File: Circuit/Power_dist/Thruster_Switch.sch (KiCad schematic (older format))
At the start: 7 parts, among them P1 XT60, Q1 IPD90P03P4L

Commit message: refactor Power_dist
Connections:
- net labels added: GNDPWR
- net labels removed: GND
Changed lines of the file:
@@
 	0    1    1    0
-$EndComp
-$Comp
-L GND #PWR026
-U 1 1 58E0369B
-P 6250 4800
-AR Path="/58E52973/58E0369B" Ref="#PWR026"  Part="1"
-AR Path="/58E62AD5/58E0369B" Ref="#PWR023"  Part="1"
-AR Path="/58E0048C/58E0369B" Ref="#PWR029"  Part="1"
-F 0 "#PWR029" H 6250 4550 50  0001 C CNN
-F 1 "GND" H 6250 4650 50  0000 C CNN
-F 2 "" H 6250 4800 50  0001 C CNN
-F 3 "" H 6250 4800 50  0001 C CNN
-	1    6250 4800
-	1    0    0    -1
 $EndComp
 Text HLabel 3700 2300 0    60   Input ~ 0
@@
 	5250 2500 5400 2500
 Connection ~ 5250 3050
-Connection ~ 6650 3850
 Wire Wire Line
 	6250 4450 6250 4300
-Connection ~ 6650 4750
 Wire Wire Line
 	6250 4650 6250 4800
@@
 Wire Wire Line
 	6650 3850 6250 3850
+$Comp
+L GNDPWR #PWR?
+U 1 1 5B5DEA3D
+P 6250 4800
+AR Path="/58E0048C/5B5DEA3D" Ref="#PWR?"  Part="1"
+AR Path="/58E52973/5B5DEA3D" Ref="#PWR?"  Part="1"
+F 0 "#PWR?" H 6250 4600 50  0001 C CNN
+F 1 "GNDPWR" H 6250 4670 50  0000 C CNN
+F 2 "" H 6250 4750 50  0001 C CNN
+F 3 "" H 6250 4750 50  0001 C CNN
+	1    6250 4800
+	1    0    0    -1
+$EndComp
 $EndSCHEMATC

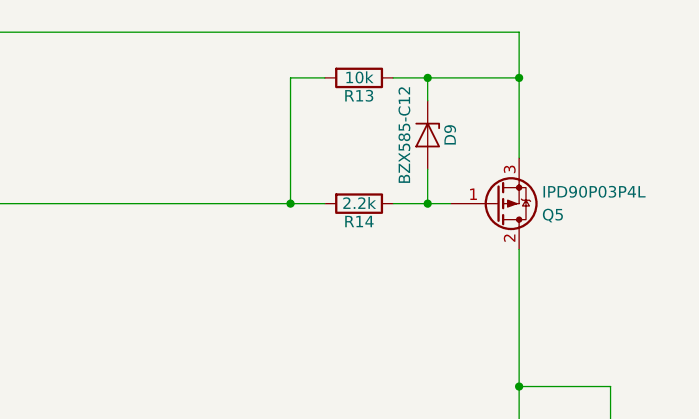
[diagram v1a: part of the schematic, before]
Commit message: changed 12V zener of Power_dist to BZT52c12s
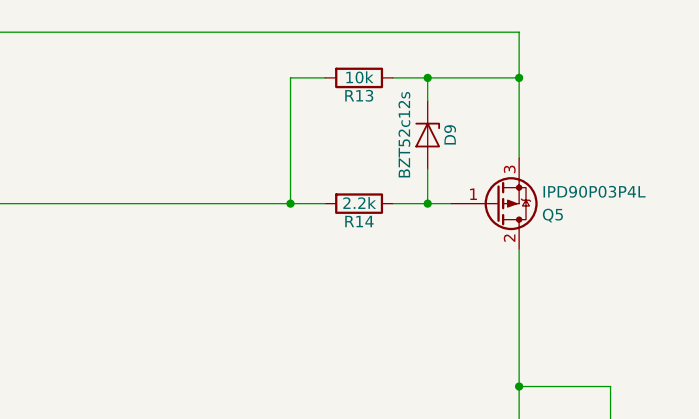
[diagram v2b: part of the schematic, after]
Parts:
- D1: value BZX585-C12 -> BZT52c12s; footprint Diodes_SMD:D_SOD-523 -> Diodes_SMD:D_SOD-323_HandSoldering
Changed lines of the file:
@@
 AR Path="/58E0048C/58E6427A" Ref="D9"  Part="1"
 F 0 "D9" H 5850 2850 50  0000 C CNN
-F 1 "BZX585-C12" H 5850 2650 50  0000 C CNN
-F 2 "Diodes_SMD:D_SOD-523" H 5850 2750 50  0001 C CNN
+F 1 "BZT52c12s" H 5850 2650 50  0000 C CNN
+F 2 "Diodes_SMD:D_SOD-323_HandSoldering" H 5850 2750 50  0001 C CNN
 F 3 "" H 5850 2750 50  0001 C CNN
 	1    5850 2750

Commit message: added 470uF to Thruster_Switch of Power_dist
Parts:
- added C?: 470uF, symbol C
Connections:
- wire segments 16 -> 18
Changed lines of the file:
@@
 	5250 3050 5250 2500
 Wire Wire Line
-	3700 2300 6250 2300
+	3700 2300 7250 2300
 Wire Wire Line
 	6250 4750 6650 4750
@@
 	1    0    0    -1
 $EndComp
+$Comp
+L C C?
+U 1 1 5B500BB4
+P 7250 2725
+F 0 "C?" H 7275 2825 50  0000 L CNN
+F 1 "470uF" H 7275 2625 50  0000 L CNN
+F 2 "" H 7288 2575 50  0001 C CNN
+F 3 "" H 7250 2725 50  0001 C CNN
+	1    7250 2725
+	1    0    0    -1
+$EndComp
+Connection ~ 6250 2300
+$Comp
+L GNDPWR #PWR?
+U 1 1 5B500D71
+P 7250 2975
+F 0 "#PWR?" H 7250 2775 50  0001 C CNN
+F 1 "GNDPWR" H 7250 2845 50  0000 C CNN
+F 2 "" H 7250 2925 50  0001 C CNN
+F 3 "" H 7250 2925 50  0001 C CNN
+	1    7250 2975
+	1    0    0    -1
+$EndComp
+Wire Wire Line
+	7250 2300 7250 2575
+Wire Wire Line
+	7250 2975 7250 2875
 $EndSCHEMATC

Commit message: changed pmos in Power_Switch_VBatt of Power_dist to STR2P3LLH6
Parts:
- removed C?: 470uF, symbol C
- added C?: 470uF, symbol C_Small
- D2: value LED_Small -> THRUSTER_SW_LED
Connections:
- net labels added: +PWR, Software_SW
- net labels removed: +Power, Software_Switch
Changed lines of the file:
@@
 $Descr A4 11693 8268
 encoding utf-8
-Sheet 5 10
+Sheet 4 10
 Title "Thruster Switch"
 Date "2017-04-06"
@@
 AR Path="/58E0048C/58E01A8B" Ref="D10"  Part="1"
 F 0 "D10" H 6200 4675 50  0000 L CNN
-F 1 "LED_Small" H 6075 4450 50  0000 L CNN
+F 1 "THRUSTER_SW_LED" H 6075 4400 50  0000 L CNN
 F 2 "LEDs:LED_0603_HandSoldering" V 6250 4550 50  0001 C CNN
 F 3 "" V 6250 4550 50  0001 C CNN
@@
 	0    1    1    0
 $EndComp
-Text HLabel 3700 2300 0    60   Input ~ 0
-+Power
-Text HLabel 3700 3050 0    60   Input ~ 0
-Software_Switch
+Text HLabel 3700 2300 0    60   UnSpc ~ 0
++PWR
+Text HLabel 3700 3050 0    60   UnSpc ~ 0
+Software_SW
 Wire Wire Line
 	6650 3850 6650 4250
@@
 	5250 3050 5250 2500
 Wire Wire Line
-	3700 2300 7250 2300
-Wire Wire Line
 	6250 4750 6650 4750
 Wire Wire Line
@@
 	1    0    0    -1
 $EndComp
-$Comp
-L C C?
-U 1 1 5B500BB4
-P 7250 2725
-F 0 "C?" H 7275 2825 50  0000 L CNN
-F 1 "470uF" H 7275 2625 50  0000 L CNN
-F 2 "" H 7288 2575 50  0001 C CNN
-F 3 "" H 7250 2725 50  0001 C CNN
-	1    7250 2725
-	1    0    0    -1
-$EndComp
 Connection ~ 6250 2300
 $Comp
 L GNDPWR #PWR?
 U 1 1 5B500D71
-P 7250 2975
-F 0 "#PWR?" H 7250 2775 50  0001 C CNN
-F 1 "GNDPWR" H 7250 2845 50  0000 C CNN
-F 2 "" H 7250 2925 50  0001 C CNN
-F 3 "" H 7250 2925 50  0001 C CNN
-	1    7250 2975
+P 6500 2675
+AR Path="/58E0048C/5B500D71" Ref="#PWR?"  Part="1"
+AR Path="/58E52973/5B500D71" Ref="#PWR?"  Part="1"
+F 0 "#PWR?" H 6500 2475 50  0001 C CNN
+F 1 "GNDPWR" H 6500 2545 50  0000 C CNN
+F 2 "" H 6500 2625 50  0001 C CNN
+F 3 "" H 6500 2625 50  0001 C CNN
+	1    6500 2675
 	1    0    0    -1
 $EndComp
 Wire Wire Line
-	7250 2300 7250 2575
+	6500 2675 6500 2600
 Wire Wire Line
-	7250 2975 7250 2875
+	3700 2300 6500 2300
+$Comp
+L C_Small C?
+U 1 1 5B5067F0
+P 6500 2500
+F 0 "C?" H 6510 2570 50  0000 L CNN
+F 1 "470uF" H 6510 2420 50  0000 L CNN
+F 2 "" H 6500 2500 50  0001 C CNN
+F 3 "" H 6500 2500 50  0001 C CNN
+	1    6500 2500
+	1    0    0    -1
+$EndComp
+Wire Wire Line
+	6500 2300 6500 2400
 $EndSCHEMATC

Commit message: added 47uF capacitor to Power_Switch_VBatt of Power_dist
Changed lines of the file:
@@
 $Descr A4 11693 8268
 encoding utf-8
-Sheet 4 10
+Sheet 2 10
 Title "Thruster Switch"
 Date "2017-04-06"
@@
 AR Path="/58E62AD5/58E019DD" Ref="P7"  Part="1"
 AR Path="/58E0048C/58E019DD" Ref="P11"  Part="1"
-F 0 "P11" H 6850 4450 50  0000 C CNN
+F 0 "P1" H 6850 4450 50  0000 C CNN
 F 1 "XT60" H 6850 4150 50  0000 C CNN
 F 2 "zeabus:XT60" H 6950 4050 60  0001 C CNN
@@
 AR Path="/58E62AD5/58E01A68" Ref="R12"  Part="1"
 AR Path="/58E0048C/58E01A68" Ref="R15"  Part="1"
-F 0 "R15" V 6330 4150 50  0000 C CNN
+F 0 "R3" V 6330 4150 50  0000 C CNN
 F 1 "10k" V 6250 4150 50  0000 C CNN
 F 2 "Resistors_SMD:R_0603_HandSoldering" V 6180 4150 50  0001 C CNN
@@
 AR Path="/58E62AD5/58E01A8B" Ref="D8"  Part="1"
 AR Path="/58E0048C/58E01A8B" Ref="D10"  Part="1"
-F 0 "D10" H 6200 4675 50  0000 L CNN
+F 0 "D2" H 6200 4675 50  0000 L CNN
 F 1 "THRUSTER_SW_LED" H 6075 4400 50  0000 L CNN
 F 2 "LEDs:LED_0603_HandSoldering" V 6250 4550 50  0001 C CNN
@@
 AR Path="/58E62AD5/58E01FA8" Ref="R10"  Part="1"
 AR Path="/58E0048C/58E01FA8" Ref="R13"  Part="1"
-F 0 "R13" V 5630 2500 50  0000 C CNN
+F 0 "R1" V 5630 2500 50  0000 C CNN
 F 1 "10k" V 5550 2500 50  0000 C CNN
 F 2 "Resistors_SMD:R_0603_HandSoldering" V 5480 2500 50  0001 C CNN
@@
 AR Path="/58E62AD5/58E01FFB" Ref="R11"  Part="1"
 AR Path="/58E0048C/58E01FFB" Ref="R14"  Part="1"
-F 0 "R14" V 5630 3050 50  0000 C CNN
+F 0 "R2" V 5630 3050 50  0000 C CNN
 F 1 "2.2k" V 5550 3050 50  0000 C CNN
 F 2 "Resistors_SMD:R_0603_HandSoldering" V 5480 3050 50  0001 C CNN
@@
 AR Path="/58E62AD5/58E51C6A" Ref="Q4"  Part="1"
 AR Path="/58E0048C/58E51C6A" Ref="Q5"  Part="1"
-F 0 "Q5" H 6350 3100 50  0000 L CNN
+F 0 "Q1" H 6350 3100 50  0000 L CNN
 F 1 "IPD90P03P4L" H 6350 3000 50  0000 L CNN
 F 2 "TO_SOT_Packages_SMD:TO-252-2" H 6350 3150 50  0001 C CNN
@@
 AR Path="/58E62AD5/58E6427A" Ref="D7"  Part="1"
 AR Path="/58E0048C/58E6427A" Ref="D9"  Part="1"
-F 0 "D9" H 5850 2850 50  0000 C CNN
+F 0 "D1" H 5850 2850 50  0000 C CNN
 F 1 "BZT52c12s" H 5850 2650 50  0000 C CNN
 F 2 "Diodes_SMD:D_SOD-323_HandSoldering" H 5850 2750 50  0001 C CNN
@@
 U 1 1 5B5067F0
 P 6500 2500
+AR Path="/58E0048C/5B5067F0" Ref="C?"  Part="1"
+AR Path="/58E52973/5B5067F0" Ref="C?"  Part="1"
 F 0 "C?" H 6510 2570 50  0000 L CNN
 F 1 "470uF" H 6510 2420 50  0000 L CNN

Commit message: added 1uF capacitor for LM4014CF in Current_Monitor of Power_dist
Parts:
- removed C?: 470uF, symbol C_Small
- added C?: 470uF, symbol CP_Small
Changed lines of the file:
@@
 $Descr A4 11693 8268
 encoding utf-8
-Sheet 11 11
+Sheet 8 11
 Title "Thruster Switch"
 Date "2017-04-06"
@@
 Wire Wire Line
 	3700 2300 6500 2300
-$Comp
-L C_Small C?
-U 1 1 5B5067F0
+Wire Wire Line
+	6500 2300 6500 2400
+$Comp
+L CP_Small C?
+U 1 1 5B531C7E
 P 6500 2500
-AR Path="/58E0048C/5B5067F0" Ref="C?"  Part="1"
-AR Path="/58E52973/5B5067F0" Ref="C?"  Part="1"
-AR Path="/5B53D7CB/5B5067F0" Ref="C?"  Part="1"
+AR Path="/58E0048C/5B531C7E" Ref="C?"  Part="1"
+AR Path="/5B53D7CB/5B531C7E" Ref="C?"  Part="1"
 F 0 "C?" H 6510 2570 50  0000 L CNN
 F 1 "470uF" H 6510 2420 50  0000 L CNN
@@
 	1    0    0    -1
 $EndComp
-Wire Wire Line
-	6500 2300 6500 2400
 $EndSCHEMATC

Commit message: Power_dist could be monitor battery voltage and system current
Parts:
- removed D1: BZT52c12s, Diodes_SMD:D_SOD-323_HandSoldering, symbol D_Zener
- added C5: 220uF, Capacitors_SMD:CP_Elec_6.3x7.7, symbol CP_Small
- added D8: BZT52c12s, Diodes_SMD:D_SOD-323_HandSoldering, symbol D_Zener_Small
- C4: renamed from C?; value 470uF -> 220uF; footprint (none) -> Capacitors_SMD:CP_Elec_6.3x7.7
- renumbered D2 to D9, P1 to P3, R1 to R17, R2 to R18, R3 to R19
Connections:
- wire segments 18 -> 21
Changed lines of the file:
@@
 $EndDescr
 $Comp
-L XT60 P1
+L XT60 P3
 U 1 1 58E019DD
 P 6850 4300
-AR Path="/58E52973/58E019DD" Ref="P1"  Part="1"
-AR Path="/58E62AD5/58E019DD" Ref="P7"  Part="1"
-AR Path="/58E0048C/58E019DD" Ref="P11"  Part="1"
-AR Path="/5B53D7CB/58E019DD" Ref="P1"  Part="1"
-F 0 "P1" H 6850 4450 50  0000 C CNN
+AR Path="/58E52973/58E019DD" Ref="P3"  Part="1"
+AR Path="/58E0048C/58E019DD" Ref="P4"  Part="1"
+AR Path="/5B53D7CB/58E019DD" Ref="P7"  Part="1"
+F 0 "P7" H 6850 4450 50  0000 C CNN
 F 1 "XT60" H 6850 4150 50  0000 C CNN
 F 2 "zeabus:XT60" H 6950 4050 60  0001 C CNN
@@
 $EndComp
 $Comp
-L R R3
+L R R19
 U 1 1 58E01A68
 P 6250 4150
-AR Path="/58E52973/58E01A68" Ref="R3"  Part="1"
-AR Path="/58E62AD5/58E01A68" Ref="R12"  Part="1"
-AR Path="/58E0048C/58E01A68" Ref="R15"  Part="1"
-AR Path="/5B53D7CB/58E01A68" Ref="R3"  Part="1"
-F 0 "R3" V 6330 4150 50  0000 C CNN
+AR Path="/58E52973/58E01A68" Ref="R19"  Part="1"
+AR Path="/58E0048C/58E01A68" Ref="R22"  Part="1"
+AR Path="/5B53D7CB/58E01A68" Ref="R40"  Part="1"
+F 0 "R40" V 6330 4150 50  0000 C CNN
 F 1 "10k" V 6250 4150 50  0000 C CNN
 F 2 "Resistors_SMD:R_0603_HandSoldering" V 6180 4150 50  0001 C CNN
@@
 $EndComp
 $Comp
-L LED_Small D2
+L LED_Small D9
 U 1 1 58E01A8B
 P 6250 4550
-AR Path="/58E52973/58E01A8B" Ref="D2"  Part="1"
-AR Path="/58E62AD5/58E01A8B" Ref="D8"  Part="1"
-AR Path="/58E0048C/58E01A8B" Ref="D10"  Part="1"
-AR Path="/5B53D7CB/58E01A8B" Ref="D2"  Part="1"
-F 0 "D2" H 6200 4675 50  0000 L CNN
+AR Path="/58E52973/58E01A8B" Ref="D9"  Part="1"
+AR Path="/58E0048C/58E01A8B" Ref="D11"  Part="1"
+AR Path="/5B53D7CB/58E01A8B" Ref="D18"  Part="1"
+F 0 "D18" H 6200 4675 50  0000 L CNN
 F 1 "THRUSTER_SW_LED" H 6075 4400 50  0000 L CNN
 F 2 "LEDs:LED_0603_HandSoldering" V 6250 4550 50  0001 C CNN
@@
 $EndComp
 $Comp
-L R R1
+L R R17
 U 1 1 58E01FA8
 P 5550 2500
-AR Path="/58E52973/58E01FA8" Ref="R1"  Part="1"
-AR Path="/58E62AD5/58E01FA8" Ref="R10"  Part="1"
-AR Path="/58E0048C/58E01FA8" Ref="R13"  Part="1"
-AR Path="/5B53D7CB/58E01FA8" Ref="R1"  Part="1"
-F 0 "R1" V 5630 2500 50  0000 C CNN
+AR Path="/58E52973/58E01FA8" Ref="R17"  Part="1"
+AR Path="/58E0048C/58E01FA8" Ref="R20"  Part="1"
+AR Path="/5B53D7CB/58E01FA8" Ref="R38"  Part="1"
+F 0 "R38" V 5630 2500 50  0000 C CNN
 F 1 "10k" V 5550 2500 50  0000 C CNN
 F 2 "Resistors_SMD:R_0603_HandSoldering" V 5480 2500 50  0001 C CNN
@@
 $EndComp
 $Comp
-L R R2
+L R R18
 U 1 1 58E01FFB
 P 5550 3050
-AR Path="/58E52973/58E01FFB" Ref="R2"  Part="1"
-AR Path="/58E62AD5/58E01FFB" Ref="R11"  Part="1"
-AR Path="/58E0048C/58E01FFB" Ref="R14"  Part="1"
-AR Path="/5B53D7CB/58E01FFB" Ref="R2"  Part="1"
-F 0 "R2" V 5630 3050 50  0000 C CNN
+AR Path="/58E52973/58E01FFB" Ref="R18"  Part="1"
+AR Path="/58E0048C/58E01FFB" Ref="R21"  Part="1"
+AR Path="/5B53D7CB/58E01FFB" Ref="R39"  Part="1"
+F 0 "R39" V 5630 3050 50  0000 C CNN
 F 1 "2.2k" V 5550 3050 50  0000 C CNN
 F 2 "Resistors_SMD:R_0603_HandSoldering" V 5480 3050 50  0001 C CNN
@@
 P 6150 3050
 AR Path="/58E52973/58E51C6A" Ref="Q1"  Part="1"
-AR Path="/58E62AD5/58E51C6A" Ref="Q4"  Part="1"
-AR Path="/58E0048C/58E51C6A" Ref="Q5"  Part="1"
-AR Path="/5B53D7CB/58E51C6A" Ref="Q1"  Part="1"
-F 0 "Q1" H 6350 3100 50  0000 L CNN
+AR Path="/58E0048C/58E51C6A" Ref="Q2"  Part="1"
+AR Path="/5B53D7CB/58E51C6A" Ref="Q7"  Part="1"
+F 0 "Q7" H 6350 3100 50  0000 L CNN
 F 1 "IPD90P03P4L" H 6350 3000 50  0000 L CNN
 F 2 "TO_SOT_Packages_SMD:TO-252-2" H 6350 3150 50  0001 C CNN
@@
 	1    0    0    1
 $EndComp
-$Comp
-L D_Zener D1
-U 1 1 58E6427A
-P 5850 2750
-AR Path="/58E52973/58E6427A" Ref="D1"  Part="1"
-AR Path="/58E62AD5/58E6427A" Ref="D7"  Part="1"
-AR Path="/58E0048C/58E6427A" Ref="D9"  Part="1"
-AR Path="/5B53D7CB/58E6427A" Ref="D1"  Part="1"
-F 0 "D1" H 5850 2850 50  0000 C CNN
-F 1 "BZT52c12s" H 5850 2650 50  0000 C CNN
-F 2 "Diodes_SMD:D_SOD-323_HandSoldering" H 5850 2750 50  0001 C CNN
-F 3 "" H 5850 2750 50  0001 C CNN
-	1    5850 2750
-	0    1    1    0
-$EndComp
-Wire Wire Line
-	5850 2600 5850 2500
+Wire Wire Line
+	5850 2500 5850 2650
 Connection ~ 5850 2500
 Wire Wire Line
-	5850 2900 5850 3050
+	5850 2850 5850 3050
 Connection ~ 5850 3050
 Connection ~ 6250 4750
@@
 	6650 3850 6250 3850
 $Comp
-L GNDPWR #PWR?
+L GNDPWR #PWR44
 U 1 1 5B5DEA3D
 P 6250 4800
-AR Path="/58E0048C/5B5DEA3D" Ref="#PWR?"  Part="1"
-AR Path="/58E52973/5B5DEA3D" Ref="#PWR?"  Part="1"
-AR Path="/5B53D7CB/5B5DEA3D" Ref="#PWR?"  Part="1"
-F 0 "#PWR?" H 6250 4600 50  0001 C CNN
+AR Path="/58E52973/5B5DEA3D" Ref="#PWR44"  Part="1"
+AR Path="/58E0048C/5B5DEA3D" Ref="#PWR46"  Part="1"
+AR Path="/5B53D7CB/5B5DEA3D" Ref="#PWR72"  Part="1"
+F 0 "#PWR72" H 6250 4600 50  0001 C CNN
 F 1 "GNDPWR" H 6250 4670 50  0000 C CNN
 F 2 "" H 6250 4750 50  0001 C CNN
@@
 Connection ~ 6250 2300
 $Comp
-L GNDPWR #PWR?
+L GNDPWR #PWR45
 U 1 1 5B500D71
-P 6500 2675
-AR Path="/58E0048C/5B500D71" Ref="#PWR?"  Part="1"
-AR Path="/58E52973/5B500D71" Ref="#PWR?"  Part="1"
-AR Path="/5B53D7CB/5B500D71" Ref="#PWR?"  Part="1"
-F 0 "#PWR?" H 6500 2475 50  0001 C CNN
-F 1 "GNDPWR" H 6500 2545 50  0000 C CNN
-F 2 "" H 6500 2625 50  0001 C CNN
-F 3 "" H 6500 2625 50  0001 C CNN
-	1    6500 2675
-	1    0    0    -1
-$EndComp
-Wire Wire Line
-	6500 2675 6500 2600
-Wire Wire Line
-	3700 2300 6500 2300
+P 6900 2700
+AR Path="/58E52973/5B500D71" Ref="#PWR45"  Part="1"
+AR Path="/58E0048C/5B500D71" Ref="#PWR47"  Part="1"
+AR Path="/5B53D7CB/5B500D71" Ref="#PWR73"  Part="1"
+F 0 "#PWR73" H 6900 2500 50  0001 C CNN
+F 1 "GNDPWR" H 6900 2570 50  0000 C CNN
+F 2 "" H 6900 2650 50  0001 C CNN
+F 3 "" H 6900 2650 50  0001 C CNN
+	1    6900 2700
+	1    0    0    -1
+$EndComp
+Wire Wire Line
+	3700 2300 6900 2300
 Wire Wire Line
 	6500 2300 6500 2400
 $Comp
-L CP_Small C?
+L CP_Small C4
 U 1 1 5B531C7E
 P 6500 2500
-AR Path="/58E0048C/5B531C7E" Ref="C?"  Part="1"
-AR Path="/5B53D7CB/5B531C7E" Ref="C?"  Part="1"
-F 0 "C?" H 6510 2570 50  0000 L CNN
-F 1 "470uF" H 6510 2420 50  0000 L CNN
-F 2 "" H 6500 2500 50  0001 C CNN
+AR Path="/58E52973/5B531C7E" Ref="C4"  Part="1"
+AR Path="/58E0048C/5B531C7E" Ref="C6"  Part="1"
+AR Path="/5B53D7CB/5B531C7E" Ref="C21"  Part="1"
+F 0 "C21" H 6510 2570 50  0000 L CNN
+F 1 "220uF" H 6510 2420 50  0000 L CNN
+F 2 "Capacitors_SMD:CP_Elec_6.3x7.7" H 6500 2500 50  0001 C CNN
 F 3 "" H 6500 2500 50  0001 C CNN
 	1    6500 2500
 	1    0    0    -1
 $EndComp
+$Comp
+L D_Zener_Small D8
+U 1 1 5B5AE897
+P 5850 2750
+AR Path="/58E52973/5B5AE897" Ref="D8"  Part="1"
+AR Path="/58E0048C/5B5AE897" Ref="D10"  Part="1"
+AR Path="/5B53D7CB/5B5AE897" Ref="D17"  Part="1"
+F 0 "D17" H 5850 2840 50  0000 C CNN
+F 1 "BZT52c12s" H 5850 2660 50  0000 C CNN
+F 2 "Diodes_SMD:D_SOD-323_HandSoldering" V 5850 2750 50  0001 C CNN
+F 3 "" V 5850 2750 50  0001 C CNN
+	1    5850 2750
+	0    1    1    0
+$EndComp
+$Comp
+L CP_Small C5
+U 1 1 5B60A994
+P 6900 2500
+AR Path="/58E52973/5B60A994" Ref="C5"  Part="1"
+AR Path="/58E0048C/5B60A994" Ref="C7"  Part="1"
+AR Path="/5B53D7CB/5B60A994" Ref="C22"  Part="1"
+F 0 "C22" H 6910 2570 50  0000 L CNN
+F 1 "220uF" H 6910 2420 50  0000 L CNN
+F 2 "Capacitors_SMD:CP_Elec_6.3x7.7" H 6900 2500 50  0001 C CNN
+F 3 "" H 6900 2500 50  0001 C CNN
+	1    6900 2500
+	1    0    0    -1
+$EndComp
+Wire Wire Line
+	6900 2300 6900 2400
+Connection ~ 6500 2300
+Wire Wire Line
+	6900 2600 6900 2700
+Wire Wire Line
+	6500 2600 6500 2650
+Wire Wire Line
+	6500 2650 6900 2650
+Connection ~ 6900 2650
 $EndSCHEMATC
